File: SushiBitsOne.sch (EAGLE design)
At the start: 56 parts, among them IC1 HT42B534, IC2 LM3671-3.3DBV, IC3 TPS562200DBV, J1 ARDUINO_R3, Q1 2N7002, Q2 MMBT2222A, U1 STM32F103CBT6-LQFP48, X1 32768Hz, X2 8MHz, X3 JTAG

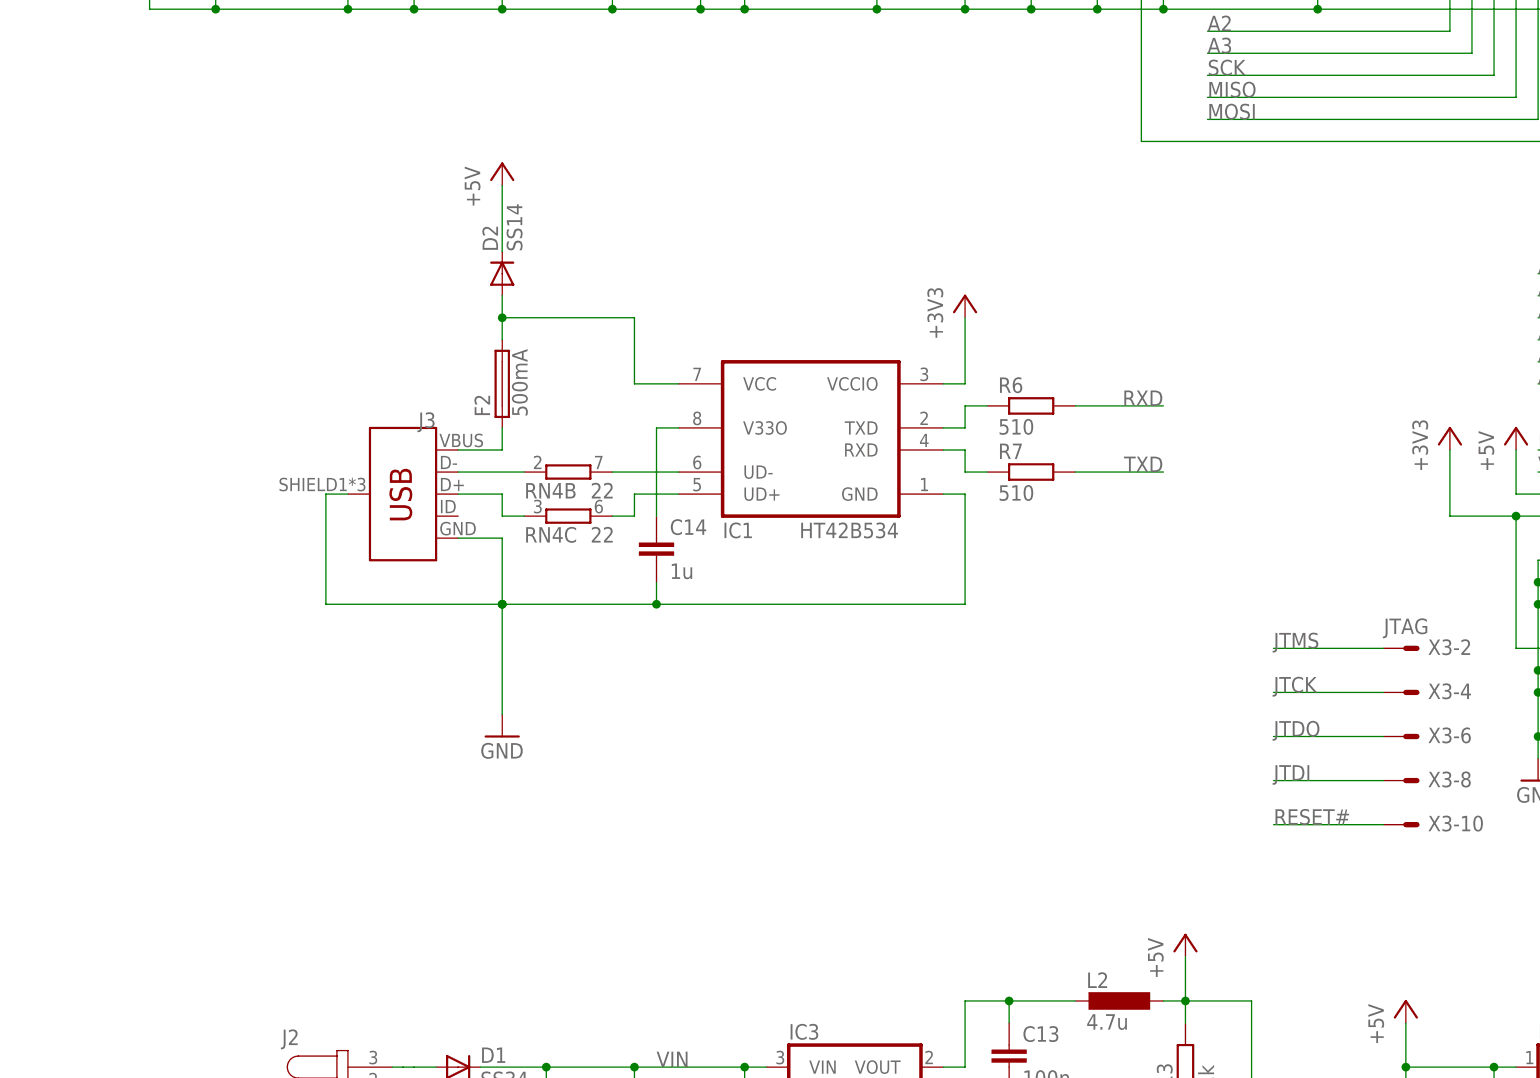
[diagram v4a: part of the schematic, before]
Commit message: Squeezed the onboard debugger back in.
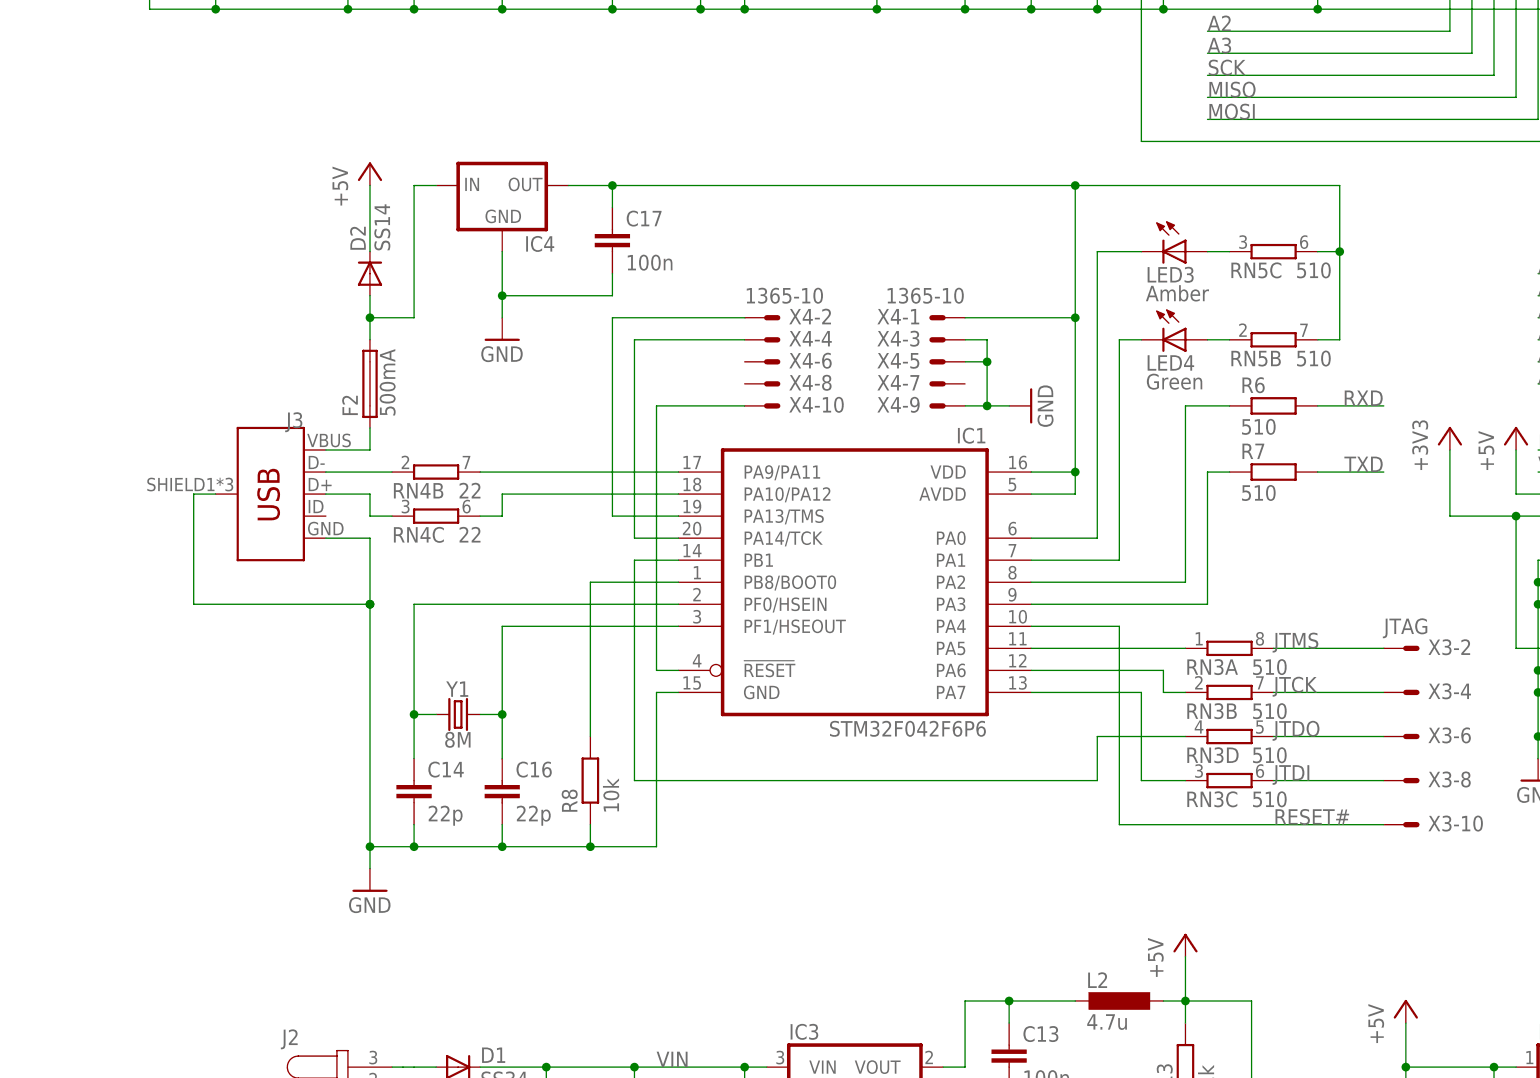
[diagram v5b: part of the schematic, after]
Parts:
- added C16: 22p, rcl:C-EUC0603
- added C17: 100n, rcl:C-EUC0603
- added IC4: (no value), v-reg:XC63FPM
- added LED3: Amber, led:LEDCHIP-LED0805
- added LED4: Green, led:LEDCHIP-LED0805
- added R8: 10k, rcl:R-EU_R0603
- added RN3, RN5: 510, resistor-dil:4R-NEXB38V
- added X4: 1365-10, con-leotronics:1365-10
- added Y1: 8M, SparkFun-Clocks:CRYSTALSMD-5X3.2-2PAD
- C14: value 1u -> 22p
- IC1: value HT42B534 -> STM32F042F6P6; device HT42B534:HT42B534 -> HeadphoneBT:STM32F042F6P6
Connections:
- new net N$25: IC1.PA14/TCK, X4-4.S
- new net N$26: IC1.PA13/TMS, X4-2.S
- new net N$27: C17.1, IC1.AVDD, IC1.VDD, IC4.OUT, RN5B.2, RN5C.2, X4-1.S
- new net N$28: C14.1, IC1.PF0/HSEIN, Y1.1
- new net N$29: C16.1, IC1.PF1/HSEOUT, Y1.2
- new net N$30: IC1.PA5, RN3A.1
- new net N$31: IC1.PA6, RN3B.1
- new net N$32: IC1.PA7, RN3C.1
- new net N$33: IC1.PB1, RN3D.1
- new net N$34: IC1.PB8/BOOT0, R8.2
- new net N$35: IC1.PA0, LED3.C
- new net N$36: IC1.PA1, LED4.C
- new net N$37: LED4.A, RN5B.1
- new net N$38: LED3.A, RN5C.1
- net +3V3: no longer IC1.VCCIO
- net GND: now also C16.2, C17.2, IC4.GND, R8.1, X4-3.S, X4-5.S, X4-9.S
- net JTCK: now also RN3B.2
- net JTDI: now also RN3C.2
- net JTDO: now also RN3D.2
- net JTMS: now also RN3A.2
- net N$16: now also IC4.IN; no longer IC1.VCC
- net N$21: now also IC1.!RESET, X4-10.S; no longer C14.1, IC1.V33O
- net N$3: now also IC1.PA9/PA11; no longer IC1.UD-
- net N$4: now also IC1.PA10/PA12; no longer IC1.UD+
- net N$5: now also IC1.PA2; no longer IC1.TXD
- net N$6: now also IC1.PA3; no longer IC1.RXD
- net RESET#: now also IC1.PA4
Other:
- moved on the sheet: C14, D2, F2, J3, R6, R7, RN4B, RN4C
